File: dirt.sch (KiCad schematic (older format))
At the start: 0 parts

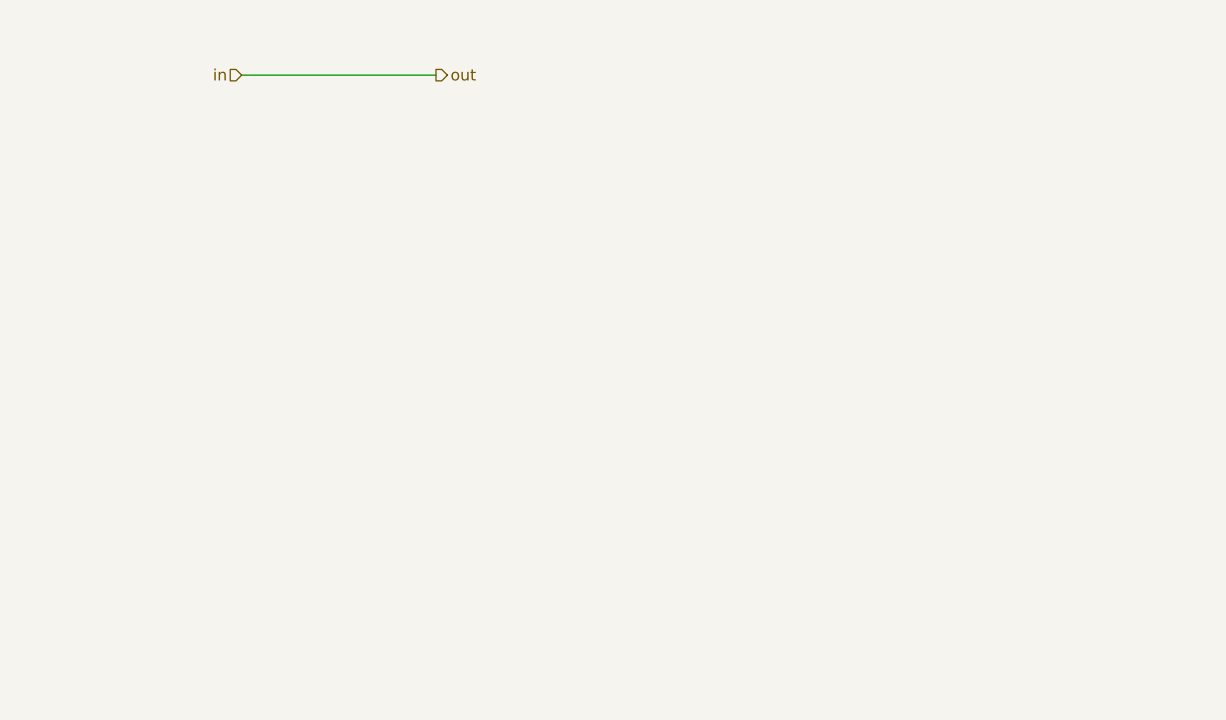
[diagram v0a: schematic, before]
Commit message: Add dirt section, some controls
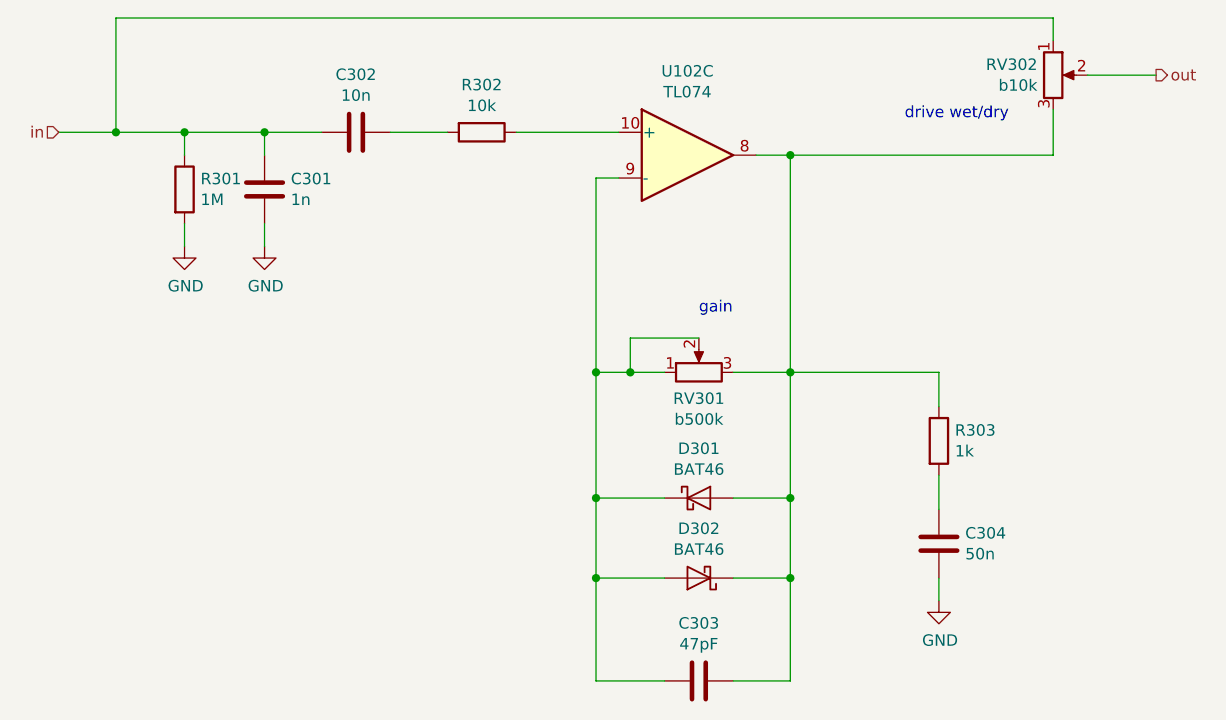
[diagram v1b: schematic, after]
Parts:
- added C301: 1n, symbol Device:C
- added C302: 10n, symbol Device:C
- added C303: 47pF, symbol Device:C
- added C304: 50n, symbol Device:C
- added D301, D302: BAT46, Diode_THT:D_DO-35_SOD27_P7.62mm_Horizontal, symbol Diode:BAT46
- added R301: 1M, symbol Device:R
- added R302: 10k, symbol Device:R
- added R303: 1k, symbol Device:R
- added RV301: b500k, symbol Device:R_POT
- added RV302: b10k, symbol Device:R_POT
- added U102: TL074, symbol Amplifier_Operational:TL074
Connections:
- net in: now also C301.1, C302.2, R301.1, RV302.1
- new net: R302.1, U102.10 (+)
- new net: C303.1, D301.2 (A), D302.1 (K), R303.1, RV301.3, RV302.3, U102.8
- new net: C303.2, D301.1 (K), D302.2 (A), RV301.1, RV301.2, U102.9 (-)
- new net: C302.1, R302.2
- new net: C304.1, R303.2
- new net GND: C301.2, C304.2, R301.2
- new net out: RV302.2
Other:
- note added: "drive wet/dry"
- note added: "gain"
